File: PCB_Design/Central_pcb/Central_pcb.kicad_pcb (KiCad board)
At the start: 2 copper layers, 37 parts, among them J1 Conn_01x06_Pin, J2 Conn_01x02_Pin, J4 Conn_01x01_Pin, J7 Barrel_Jack, U3 nRF52832-QFxx, U4 BQ25171QWDRCRQ1, U5 AMS1117-3.3

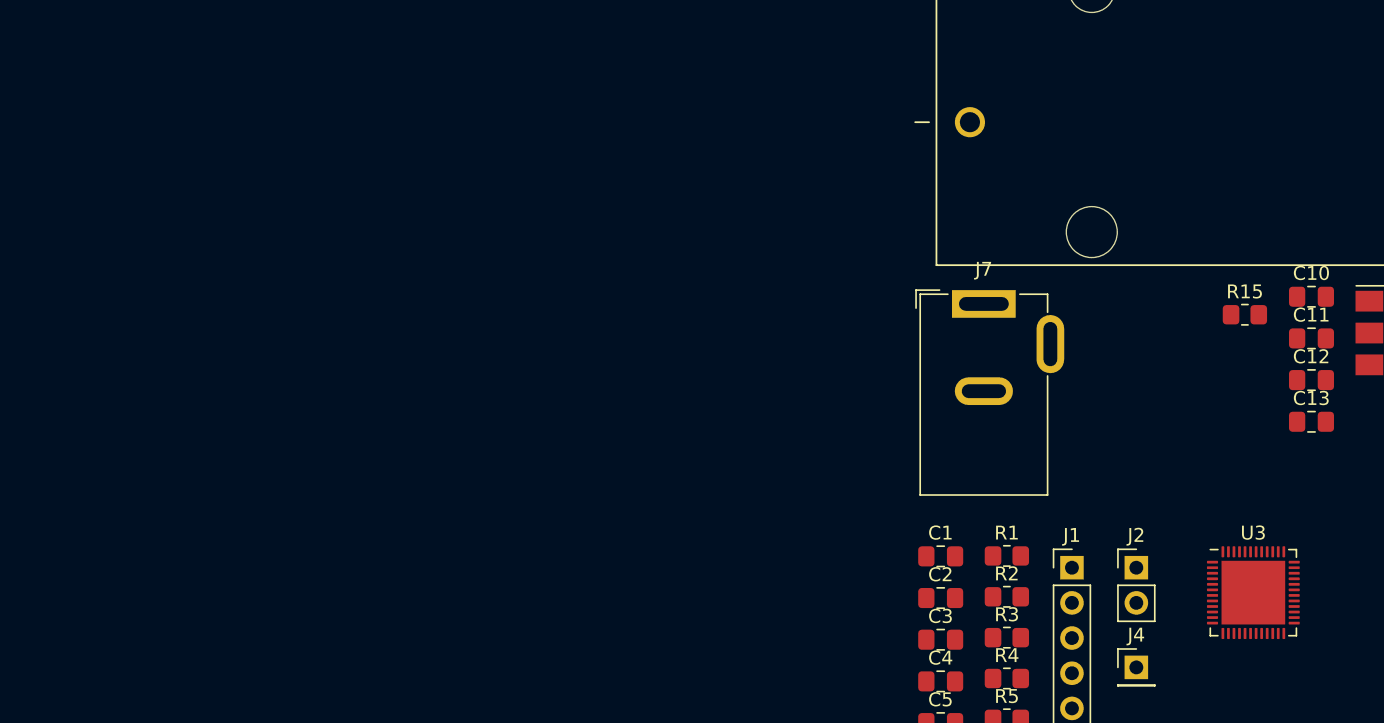
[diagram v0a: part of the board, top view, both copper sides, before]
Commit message: Scematic update
update scematic and added some footrpints
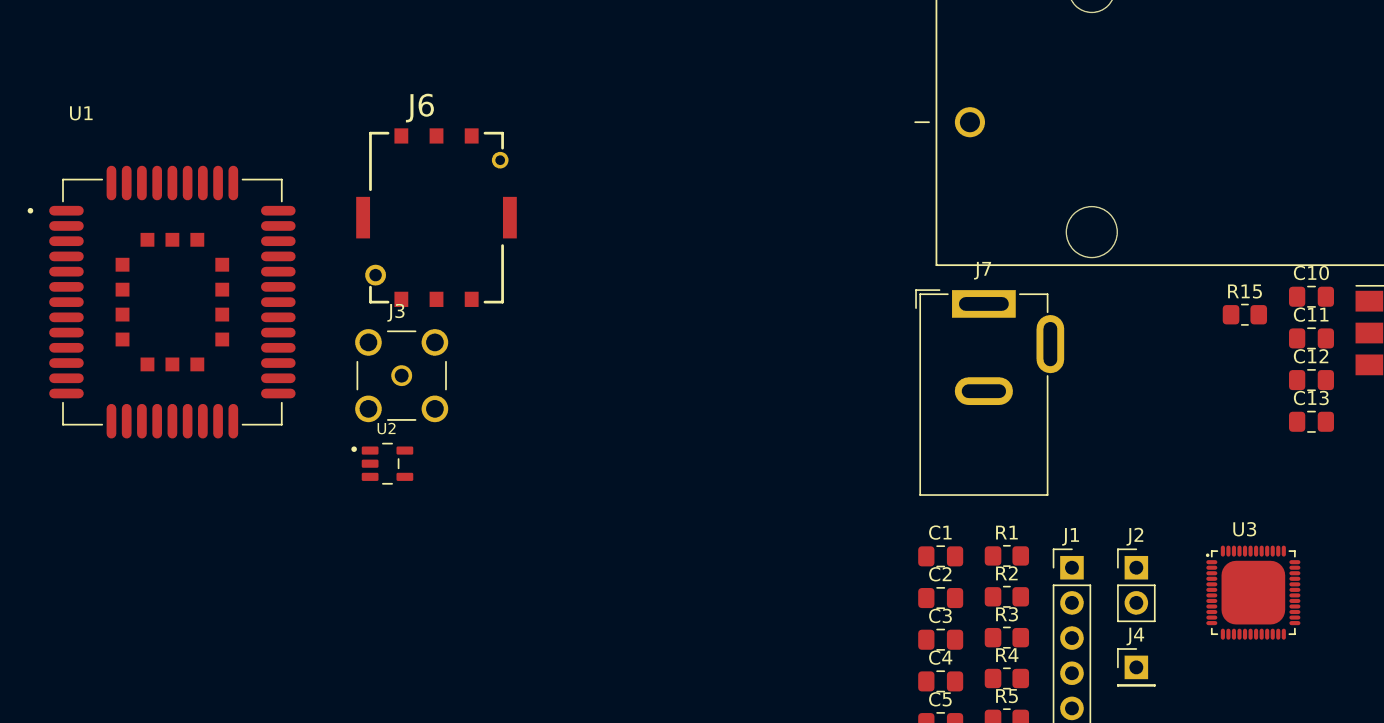
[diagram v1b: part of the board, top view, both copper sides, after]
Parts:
- added J3: SMA_CONNECTOR, Central:LPRS_SMA_CONNECTOR, F.Cu at (62.0, 116.5)
- added J6: SIM8051-6-0-14-01-X-REVD, Central:GCT_SIM8051-6-0-14-01-X-REVD, F.Cu at (64.5, 105.1)
- added U1: BC660K-GL, Central:XCVR_BC660K-GL, F.Cu at (45.4, 111.2)
- added U2: ESDS304DBVR, Central:SOT95P280X145-5N, F.Cu at (61.0, 122.9)
- D1: value LED -> STAT1
- D2: value LED -> STAT2
- U3: value nRF52832-QFxx -> NRF52832-QFAA-R; footprint Package_DFN_QFN:QFN-48-1EP_6x6mm_P0.4mm_EP4.6x4.6mm -> Central:QFN40P600X600X90-49N
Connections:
- net CE_GQ25171 renamed CE_BQ25171
- BT1 pad N1: GND -> poort45
- C1 pad 1: GND -> poort45
- C10 pad 2: GND -> poort45
- C11 pad 2: GND -> poort45
- C12 pad 1: GND -> poort45
- C13 pad 2: GND -> poort45
- C2 pad 1: GND -> poort45
- C3 pad 1: GND -> poort45
- C4 pad 1: GND -> poort45
- C5 pad 2: GND -> poort45
- C6 pad 2: GND -> poort45
- C7 pad 2: GND -> poort45
- C8 pad 2: GND -> poort45
- J7 pad 2: GND -> poort45
- R10 pad 2: GND -> poort45
- R11 pad 2: GND -> poort45
- R13 pad 2: GND -> poort45
- U3 pad 1: unconnected-(U3-DEC1-Pad1) -> Net-(U3-DEC1)
- U3 pad 13: Net-(U3-VDD-Pad13) -> +3.3V
- U3 pad 30: unconnected-(U3-ANT-Pad30) -> Net-(U3-ANT)
- U3 pad 31: Net-(U3-VSS-Pad31) -> poort45
- U3 pad 33: unconnected-(U3-DEC3-Pad33) -> Net-(U3-DEC3)
- U3 pad 34: unconnected-(U3-XC1-Pad34) -> Net-(U3-XC1)
- U3 pad 35: unconnected-(U3-XC2-Pad35) -> xc2
- U3 pad 36: Net-(U3-VDD-Pad13) -> +3.3V
- U3 pad 44: unconnected-(U3-NC-Pad44) -> (no net)
- U3 pad 45: Net-(U3-VSS-Pad31) -> poort45
- U3 pad 46: unconnected-(U3-DEC4-Pad46) -> Net-(U3-DEC4)
- U3 pad 48: Net-(U3-VDD-Pad13) -> +3.3V
- U3 pad 49: Net-(U3-VSS-Pad31) -> unconnected-(U3-EXP-Pad49)
- U4 pad 5: GND -> poort45
- U5 pad 1: GND -> poort45

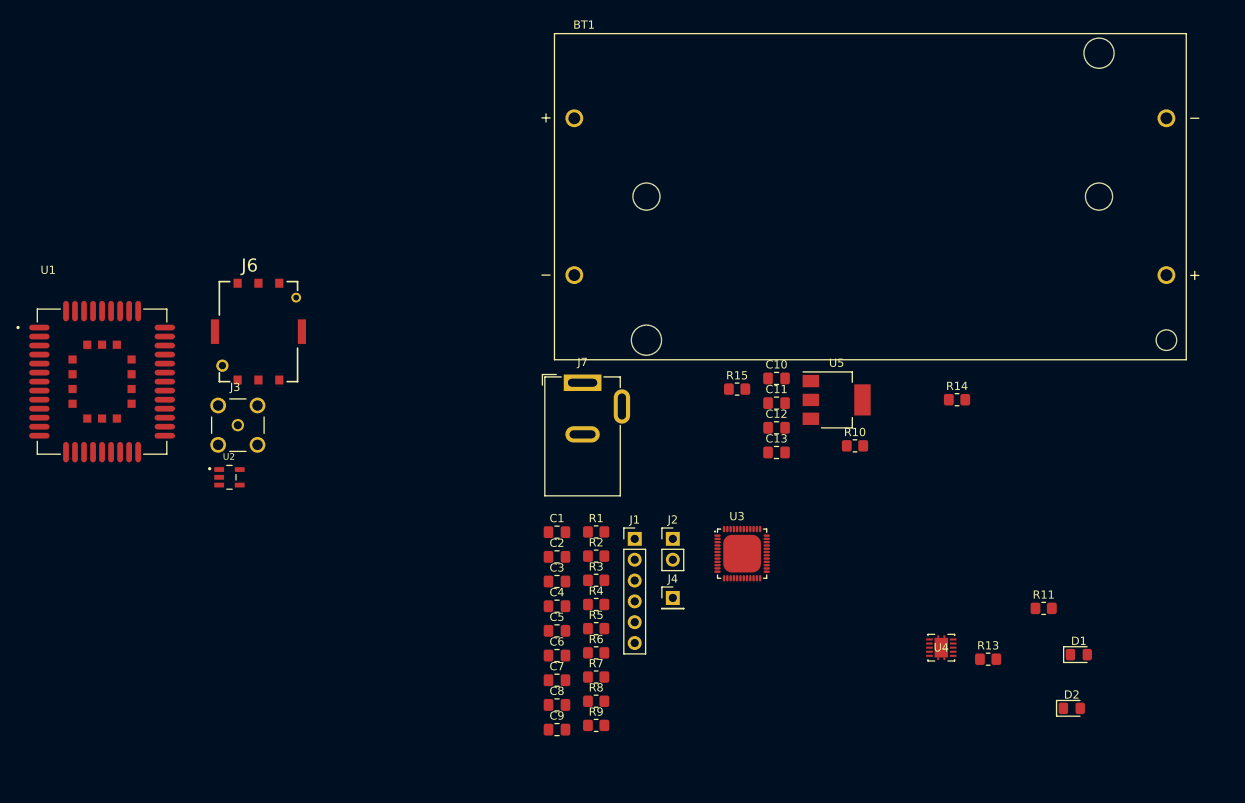
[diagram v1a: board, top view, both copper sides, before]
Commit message: Initial PCB design
Rough sketch of what the layout could be
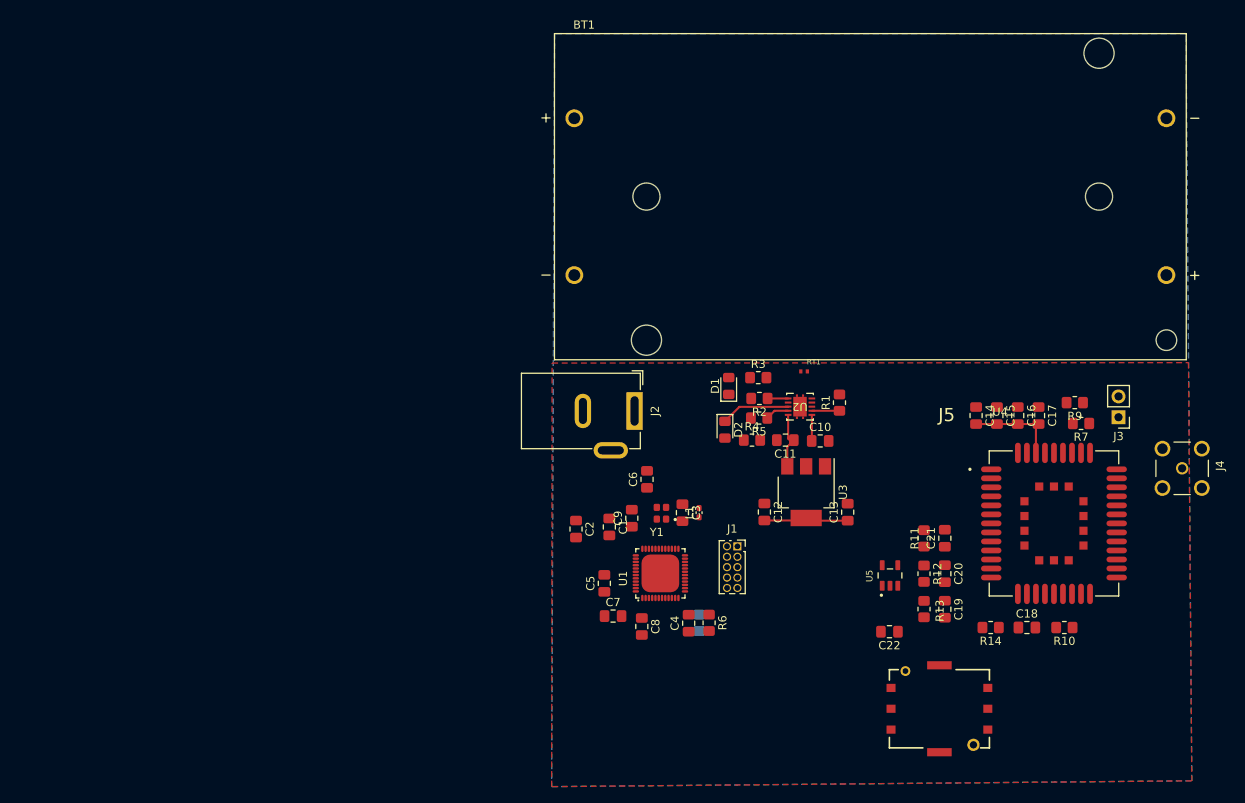
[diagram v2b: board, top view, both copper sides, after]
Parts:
- removed J6: SIM8051-6-0-14-01-X-REVD, Central:GCT_SIM8051-6-0-14-01-X-REVD
- removed J7: Barrel_Jack, Connector_BarrelJack:BarrelJack_GCT_DCJ200-10-A_Horizontal
- removed R15: 10K, Resistor_SMD:R_0805_2012Metric_Pad1.20x1.40mm_HandSolder
- added C14: 100µ, Capacitor_SMD:C_0805_2012Metric_Pad1.18x1.45mm_HandSolder, F.Cu at (152.0, 115.4)
- added C15: 100n, Capacitor_SMD:C_0805_2012Metric_Pad1.18x1.45mm_HandSolder, F.Cu at (154.6, 115.4)
- added C16: 100p, Capacitor_SMD:C_0805_2012Metric_Pad1.18x1.45mm_HandSolder, F.Cu at (157.1, 115.4)
- added C17: 22p, Capacitor_SMD:C_0805_2012Metric_Pad1.18x1.45mm_HandSolder, F.Cu at (159.7, 115.4)
- added C18: 33p, Capacitor_SMD:C_0805_2012Metric_Pad1.18x1.45mm_HandSolder, F.Cu at (158.2, 141.2)
- added C19: 33p, Capacitor_SMD:C_0805_2012Metric_Pad1.18x1.45mm_HandSolder, F.Cu at (148.2, 139.0)
- added C20: 33p, Capacitor_SMD:C_0805_2012Metric_Pad1.18x1.45mm_HandSolder, F.Cu at (148.2, 134.7)
- added C21: 33p, Capacitor_SMD:C_0805_2012Metric_Pad1.18x1.45mm_HandSolder, F.Cu at (148.2, 130.3)
- added C22: 100n, Capacitor_SMD:C_0805_2012Metric_Pad1.18x1.45mm_HandSolder, F.Cu at (141.5, 141.7)
- added J5: SIM8051-6-0-14-01-X-REVD, Central:GCT_SIM8051-6-0-14-01-X-REVD, F.Cu at (147.6, 151.1)
- added L1: 3.9n, Capacitor_SMD:C_0402_1005Metric_Pad0.74x0.62mm_HandSolder, F.Cu at (118.3, 127.2)
- added R12: 22, Resistor_SMD:R_0805_2012Metric_Pad1.20x1.40mm_HandSolder, F.Cu at (145.7, 134.7)
- added RT1: NTCG103JF103FT1, Central:THERM_NTCG103JF103FT1, F.Cu at (131.1, 110.0)
- added Y1: CX2016DB32000D0WZRC1, Central:OSCCC200X160X45N, F.Cu at (113.7, 127.3)
- C1: value 100µ -> 12pF
- C2: value 100n -> 12pF
- C3: value 100p -> 0.8p
- C4: value 22p -> 100n
- C5: value 33p -> 1u
- C6: value 33p -> 100p
- C7: value 33p -> 4.7u
- C8: value 33p -> 100n
- J1: value Conn_01x06_Pin -> Conn_ARM_JTAG_SWD_10; footprint Connector_PinHeader_2.54mm:PinHeader_1x06_P2.54mm_Vertical -> Connector_PinSocket_1.27mm:PinSocket_2x05_P1.27mm_Vertical
- J2: value Conn_01x02_Pin -> Barrel_Jack; footprint Connector_PinHeader_2.54mm:PinHeader_1x02_P2.54mm_Vertical -> Connector_BarrelJack:BarrelJack_GCT_DCJ200-10-A_Horizontal
- J3: value SMA_CONNECTOR -> Conn_01x02_Pin; footprint Central:LPRS_SMA_CONNECTOR -> Connector_PinHeader_2.54mm:PinHeader_1x02_P2.54mm_Vertical
- J4: value Conn_01x01_Pin -> SMA_CONNECTOR; footprint Connector_PinHeader_2.54mm:PinHeader_1x01_P2.54mm_Vertical -> Central:LPRS_SMA_CONNECTOR
- R1: value 1k -> 600
- R10: value 3.6K -> 1k
- R11: value 600 -> 22
- R13: value 100K -> 22
- R14: value 10K -> 10k
- R2: value 1k -> 100K
- R3, R4: value 1k -> 10K
- R5: value 1k -> 3.6K
- R6, R7: value 22 -> 1k
- R8: value 22 -> 1k; moved to B.Cu
- R9: value 10k -> 1k
- U1: value BC660K-GL -> NRF52832-QFAA-R; footprint Central:XCVR_BC660K-GL -> Central:QFN40P600X600X90-49N
- U2: value ESDS304DBVR -> BQ25171QWDRCRQ1; footprint Central:SOT95P280X145-5N -> Central:VSON10_BQ25171_3X3_TEX
- U3: value NRF52832-QFAA-R -> AMS1117-3.3; footprint Central:QFN40P600X600X90-49N -> Package_TO_SOT_SMD:SOT-223-3_TabPin2
- U4: value BQ25171QWDRCRQ1 -> BC660K-GL; footprint Central:VSON10_BQ25171_3X3_TEX -> Central:XCVR_BC660K-GL
- U5: value AMS1117-3.3 -> ESDS304DBVR; footprint Package_TO_SOT_SMD:SOT-223-3_TabPin2 -> Central:SOT95P280X145-5N
- moved J3 107.4 mm to (169.4, 115.6), turned to 180 degrees
- moved U1 72.0 mm to (113.5, 134.6), turned to 90 degrees
- moved R9 70.4 mm to (164.1, 113.8), turned to 180 degrees
- moved U2 70.1 mm to (130.6, 114.3), turned to 180 degrees
- moved R7 66.7 mm to (164.8, 116.3), turned to 180 degrees
- moved J4 64.1 mm to (177.2, 121.8), turned to -90 degrees
- moved D2 54.3 mm to (121.4, 117.1), turned to -90 degrees
- moved D1 53.8 mm to (121.9, 111.8), turned to 90 degrees
- moved R10 33.8 mm to (162.8, 141.2), turned to 180 degrees
- moved R1 33.6 mm to (135.4, 113.8), turned to 90 degrees
- moved R5 32.5 mm to (125.6, 115.7), turned to 180 degrees
- moved R3 31.7 mm to (125.5, 110.7)
- moved R14 28.1 mm to (153.8, 141.2), turned to 180 degrees
- moved R2 27.7 mm to (125.6, 113.3), turned to 180 degrees
- moved R4 27.6 mm to (124.7, 118.4)
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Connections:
- BT1 pad N1: poort45 -> GND
- BT1 pad P2: Net-(U4-OUT) -> Net-(U2-OUT)
- C1 pad 1: poort45 -> GND
- C1 pad 2: +3.3V -> Net-(U1-XC1)
- C10 pad 1: Net-(U4-IN) -> Net-(U2-IN)
- C10 pad 2: poort45 -> GND
- C11 pad 1: Net-(U4-OUT) -> Net-(U2-OUT)
- C11 pad 2: poort45 -> GND
- C12 pad 1: poort45 -> GND
- C13 pad 2: poort45 -> GND
- C2 pad 1: poort45 -> GND
- C2 pad 2: +3.3V -> xc2
- C3 pad 1: poort45 -> GND
- C3 pad 2: +3.3V -> Net-(U1-ANT)
- C4 pad 1: poort45 -> +3.3V
- C4 pad 2: +3.3V -> GND
- C5 pad 1: Net-(J6-VCC) -> Net-(U1-DEC4)
- C5 pad 2: poort45 -> GND
- C6 pad 1: Net-(U1-USIM_CLK) -> Net-(U1-DEC3)
- C6 pad 2: poort45 -> GND
- C7 pad 1: Net-(U1-USIM_RST) -> GND
- C7 pad 2: poort45 -> +3.3V
- C8 pad 1: Net-(U1-USIM_DATA) -> Net-(U1-DEC1)
- C8 pad 2: poort45 -> GND
- C9 pad 1: Net-(J6-GND) -> +3.3V
- C9 pad 2: Net-(J6-VCC) -> GND
- J1 pad 1: Net-(J1-Pin_1) -> +3.3V
- J1 pad 2: Net-(J1-Pin_2) -> Net-(J1-SWDIO/TMS)
- J1 pad 3: Net-(J1-Pin_3) -> GND
- J1 pad 4: Net-(J1-Pin_4) -> Net-(J1-SWDCLK/TCK)
- J1 pad 5: Net-(J1-Pin_5) -> GND
- J1 pad 6: Net-(J1-Pin_6) -> SW0
- J2 pad 1: Net-(J2-Pin_1) -> Net-(U2-IN)
- J2 pad 2: Net-(J2-Pin_2) -> GND
- J3 pad 1: Net-(U1-ANT_RF) -> Net-(J3-Pin_1)
- J4 pad 1: Net-(J4-Pin_1) -> Net-(U4-ANT_RF)
- R1 pad 1: Net-(J2-Pin_1) -> Net-(U2-ISET)
- R1 pad 2: Net-(U1-DBG_RXD) -> GND
- R10 pad 1: Net-(U4-VSET) -> Net-(U4-RI)
- R10 pad 2: poort45 -> RI_BC660
- R11 pad 1: Net-(U4-ISET) -> Net-(U4-USIM_DATA)
- R11 pad 2: poort45 -> Net-(J5-I/O)
- R13 pad 1: Net-(U4-CHM_TMP) -> Net-(U4-USIM_CLK)
- R13 pad 2: poort45 -> Net-(J5-CLK)
- R14 pad 1: Net-(D1-A) -> Net-(J5-VCC)
- R14 pad 2: +3.3V -> Net-(J5-I/O)
- R2 pad 1: Net-(J1-Pin_3) -> Net-(U2-CHM_TMP)
- R2 pad 2: Net-(U1-MAIN_TXD) -> GND
- R3 pad 1: Net-(J1-Pin_4) -> Net-(D1-A)
- R3 pad 2: Net-(U1-MAIN_RXD) -> +3.3V
- R4 pad 1: Net-(J2-Pin_2) -> Net-(D2-A)
- R4 pad 2: Net-(U1-DBG_TXD) -> +3.3V
- R5 pad 1: Net-(U1-RI) -> Net-(U2-VSET)
- R5 pad 2: Net-(J1-Pin_6) -> GND
- R6 pad 1: Net-(U1-USIM_CLK) -> TXD_BC660
- R6 pad 2: Net-(J6-CLK) -> Net-(U4-MAIN_TXD)
- R7 pad 1: Net-(U1-USIM_RST) -> Net-(J3-Pin_1)
- R7 pad 2: Net-(J6-RST) -> Net-(U4-DBG_RXD)
- R8 pad 1: Net-(U1-USIM_DATA) -> RXD_BC660
- R8 pad 2: Net-(J6-I/O) -> Net-(U4-MAIN_RXD)
- R9 pad 1: Net-(J6-VCC) -> Net-(J3-Pin_2)
- R9 pad 2: Net-(J6-I/O) -> Net-(U4-DBG_TXD)
- U1 pad 1: poort45 -> Net-(U1-DEC1)
- U1 pad 10: Net-(J6-GND) -> BOOT_BC660
- U1 pad 11: Net-(U1-USIM_DATA) -> unconnected-(U1-P0.09-Pad11)
- U1 pad 12: Net-(U1-USIM_RST) -> unconnected-(U1-P0.10-Pad12)
- U1 pad 13: Net-(U1-USIM_CLK) -> +3.3V
- U1 pad 14: Net-(J6-VCC) -> RXD_BC660
- U1 pad 15: Net-(J1-Pin_1) -> TXD_BC660
- U1 pad 16: Net-(J1-Pin_2) -> RI_BC660
- U1 pad 17: Net-(U1-MAIN_TXD) -> PSM_EINT_BC660
- U1 pad 18: Net-(U1-MAIN_RXD) -> unconnected-(U1-P0.15-Pad18)
- U1 pad 19: Net-(J1-Pin_5) -> unconnected-(U1-P0.16-Pad19)
- U1 pad 20: Net-(U1-RI) -> unconnected-(U1-P0.17-Pad20)
- U1 pad 21: unconnected-(U1-RESERVED_1-Pad21) -> SW0
- U1 pad 24: unconnected-(U1-VDD_EXT-Pad24) -> Nreset
- U1 pad 25: unconnected-(U1-RESERVED_1-Pad25) -> Net-(J1-SWDCLK/TCK)
- U1 pad 26: unconnected-(U1-RESERVED_1-Pad26) -> Net-(J1-SWDIO/TMS)
- U1 pad 27: poort45 -> unconnected-(U1-P0.22-Pad27)
- U1 pad 30: unconnected-(U1-RESERVED_1-Pad30) -> Net-(U1-ANT)
- U1 pad 31: unconnected-(U1-RESERVED_1-Pad31) -> GND
- U1 pad 33: unconnected-(U1-RESERVED_1-Pad33) -> Net-(U1-DEC3)
- U1 pad 34: poort45 -> Net-(U1-XC1)
- U1 pad 35: Net-(U1-ANT_RF) -> xc2
- U1 pad 36: poort45 -> +3.3V
- U1 pad 37: poort45 -> unconnected-(U1-P0.25-Pad37)
- U1 pad 38: Net-(U1-DBG_RXD) -> unconnected-(U1-P0.26-Pad38)
- U1 pad 39: Net-(U1-DBG_TXD) -> unconnected-(U1-P0.27-Pad39)
- U1 pad 40: poort45 -> unconnected-(U1-P0.28-Pad40)
- U1 pad 41: poort45 -> unconnected-(U1-P0.29-Pad41)
- U1 pad 42: +3.3V -> unconnected-(U1-P0.30-Pad42)
- U1 pad 43: +3.3V -> unconnected-(U1-P0.31-Pad43)
- U1 pad 44: unconnected-(U1-RESERVED_1-Pad44) -> (no net)
- U1 pad 45: unconnected-(U1-RESERVED_1-Pad45) -> GND
- U1 pad 46: unconnected-(U1-RESERVED_2-Pad46) -> Net-(U1-DEC4)
- U1 pad 48: unconnected-(U1-RESERVED_2-Pad48) -> +3.3V
- U1 pad 7: Net-(J4-Pin_1) -> unconnected-(U1-P0.05-Pad7)
- U1 pad 9: unconnected-(U1-ADC0-Pad9) -> RESET_BC660
- U2 pad 1: Net-(J6-VCC) -> Net-(U2-IN)
- U2 pad 2: poort45 -> Net-(U2-ISET)
- U2 pad 3: Net-(U1-USIM_CLK) -> CE_BQ25171
- U2 pad 4: Net-(U1-USIM_RST) -> Net-(U2-TS)
- U2 pad 5: Net-(U1-USIM_DATA) -> GND
- U3 pad 1: Net-(U3-DEC1) -> GND
- U3 pad 2: unconnected-(U3-P0.00-Pad2) -> +3.3V
- U3 pad 3: unconnected-(U3-P0.01-Pad3) -> Net-(U2-OUT)
- U4 pad 1: Net-(U4-IN) -> GND
- U4 pad 10: Net-(U4-OUT) -> Net-(J5-GND)
- U4 pad 11: unconnected-(U4-Pad11) -> Net-(U4-USIM_DATA)
- U4 pad 2: Net-(U4-ISET) -> unconnected-(U4-RESERVED_1-Pad2)
- U4 pad 3: CE_BQ25171 -> unconnected-(U4-GPIO1-Pad3)
- U4 pad 4: Net-(U4-TS) -> unconnected-(U4-GPIO2-Pad4)
- U4 pad 5: poort45 -> unconnected-(U4-GPIO3-Pad5)
- U4 pad 6: Net-(U4-CHM_TMP) -> unconnected-(U4-GPIO4-Pad6)
- U4 pad 7: Net-(D1-K) -> BOOT_BC660
- U4 pad 8: Net-(D2-K) -> unconnected-(U4-RESERVED_1-Pad8)
- U4 pad 9: Net-(U4-VSET) -> unconnected-(U4-ADC0-Pad9)
- U5 pad 1: poort45 -> Net-(J5-VCC)
- U5 pad 2: +3.3V -> GND
- U5 pad 3: Net-(U4-OUT) -> Net-(U4-USIM_CLK)
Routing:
- net +3.3V: track 0.00 -> 20.3 mm
- net Net-(D2-K): track 0.00 -> 8.45 mm
- net Net-(U2-OUT): track 0.00 -> 6.69 mm
- net Net-(U2-ISET): track 0.00 -> 3.37 mm
- net Net-(U2-IN): track 0.00 -> 3.16 mm
- net Net-(U2-VSET): track 0.00 -> 2.91 mm
- net Net-(U2-CHM_TMP): track 0.00 -> 2.51 mm
- added copper zone on B.Cu, net GND
- added copper zone on F.Cu, net GND

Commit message: PCB route
Volledig geroute nog juist controleren en mounting holes doen + controleren dat er overal gnd en 3.3v mooi verbonden is
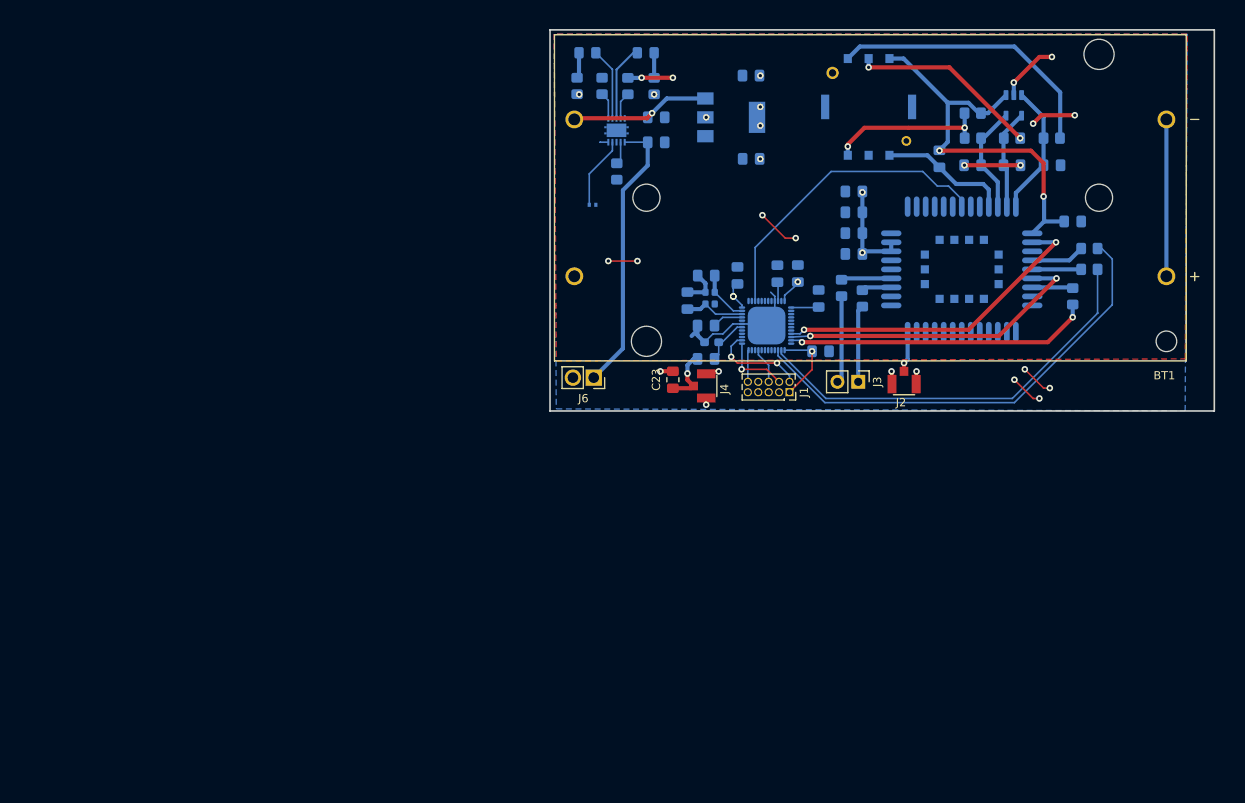
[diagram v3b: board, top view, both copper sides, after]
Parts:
- added C23: 1.2pF, Capacitor_SMD:C_0805_2012Metric_Pad1.18x1.45mm_HandSolder, F.Cu at (115.1, 111.0)
- added J6: Conn_01x02_Pin, Connector_PinSocket_2.54mm:PinSocket_1x02_P2.54mm_Vertical, F.Cu at (105.4, 110.7)
- C1, C10, C11, C12, C13, C14, C15, C16, C17, C18, C19, C2, C20, C21, C22, C4, C5, C6, C7, C8, C9, D1, D2, R10, R11, R12, R13, R14, R2, R3, R4, R5, R6, R7, R9, RT1, U1, U2, U3, U4, U5, Y1: moved to B.Cu
- C3: footprint Capacitor_SMD:C_0805_2012Metric_Pad1.18x1.45mm_HandSolder -> Capacitor_SMD:C_0603_1608Metric_Pad1.08x0.95mm_HandSolder; moved to B.Cu
- J2: value Barrel_Jack -> U.FL-R-SMT_01_; footprint Connector_BarrelJack:BarrelJack_GCT_DCJ200-10-A_Horizontal -> Central:HRS_U.FL-R-SMT_01_
- J4: value SMA_CONNECTOR -> U.FL-R-SMT_01_; footprint Central:LPRS_SMA_CONNECTOR -> Central:HRS_U.FL-R-SMT_01_
- J5: value SIM8051-6-0-14-01-X-REVD -> SIM; moved to B.Cu
- L1: footprint Capacitor_SMD:C_0402_1005Metric_Pad0.74x0.62mm_HandSolder -> Capacitor_SMD:C_0805_2012Metric_Pad1.18x1.45mm_HandSolder; moved to B.Cu
- R1: value 600 -> 3k; moved to B.Cu
- moved J5 73.9 mm to (138.9, 77.7), turned to 0 degrees
- moved R6 65.1 mm to (165.9, 95.0), turned to 180 degrees
- moved R8 64.2 mm to (165.9, 97.5), turned to 180 degrees
- moved R14 62.8 mm to (151.6, 78.5)
- moved R13 59.5 mm to (161.3, 81.5), turned to 0 degrees
- moved U5 59.3 mm to (156.6, 77.5), turned to -90 degrees
- moved J4 58.9 mm to (119.1, 111.8)
- moved C22 58.0 mm to (147.6, 84.1), turned to 90 degrees
- moved C19 55.7 mm to (161.3, 84.8), turned to 0 degrees
- moved R12 54.2 mm to (156.4, 81.5), turned to 0 degrees
- moved C12 53.3 mm to (124.6, 73.9), turned to 0 degrees
- moved C20 50.5 mm to (156.4, 84.8), turned to 0 degrees
- moved C18 49.8 mm to (163.8, 91.7)
- moved R11 49.2 mm to (151.7, 81.5), turned to 180 degrees
- moved C7 47.5 mm to (130.3, 98.0), turned to -90 degrees
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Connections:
- BT1 pad N1: GND -> Net-(BT1-PadN1)
- BT1 pad N2: Net-(BT1-PadN2) -> GND
- BT1 pad P1: Net-(BT1-PadN2) -> Net-(U2-OUT)
- BT1 pad P2: Net-(U2-OUT) -> Net-(BT1-PadN1)
- C10 pad 1: Net-(U2-IN) -> Net-(J6-Pin_1)
- J2 pad 1: Net-(U2-IN) -> GND
- J2 pad 3: (no net) -> Net-(J2-SIG)
- J4 pad 1: Net-(U4-ANT_RF) -> GND
- L1 pad 2: RF -> Net-(J4-SIG)
- U1 pad 10: BOOT_BC660 -> PSM_EINT_BC660
- U1 pad 11: unconnected-(U1-P0.09-Pad11) -> RI_BC660
- U1 pad 16: RI_BC660 -> unconnected-(U1-P0.13-Pad16)
- U1 pad 17: PSM_EINT_BC660 -> unconnected-(U1-P0.14-Pad17)
- U1 pad 39: unconnected-(U1-P0.27-Pad39) -> BOOT_BC660
- U1 pad 49: unconnected-(U1-EXP-Pad49) -> GND
- U2 pad 1: Net-(U2-IN) -> Net-(J6-Pin_1)
- U4 pad 35: Net-(U4-ANT_RF) -> Net-(J2-SIG)
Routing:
- net GND: track 0.00 -> 72.2 mm, vias 0 -> 21
- net TXD_BC660: track 0.00 -> 56.7 mm
- net RXD_BC660: track 0.00 -> 51.0 mm
- net Net-(J5-VCC): track 0.00 -> 49.1 mm, vias 0 -> 2
- net RESET_BC660: track 0.00 -> 39.8 mm, vias 0 -> 2
- net PSM_EINT_BC660: track 0.00 -> 38.2 mm, vias 0 -> 2
- net BOOT_BC660: track 0.00 -> 37.9 mm
- net RI_BC660: track 0.00 -> 37.3 mm, vias 0 -> 2
- net Net-(J5-CLK): track 0.00 -> 34.4 mm
- net Net-(J6-Pin_1): track 0.00 -> 34.2 mm
- net Net-(J5-RST): track 0.00 -> 23.1 mm, vias 0 -> 2
- net Net-(J5-I/O): track 0.00 -> 19.2 mm, vias 0 -> 2
- net Net-(BT1-PadN1): track 0.00 -> 19.1 mm
- net Net-(U4-USIM_CLK): track 0.00 -> 16.1 mm
- net Net-(J5-GND): track 0.00 -> 15.9 mm
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- added copper zone on F.Cu, net +3.3V
- removed copper zone on F.Cu, net GND
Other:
- board outline added: 81 x 46.5 mm

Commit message: Minur PCB update
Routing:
- net GND: track 72.2 -> 83.7 mm
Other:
- board size 81 x 46.5 mm -> 81.8 x 46.5 mm
- board text added: "Iot systems by:Jarno de Jonckheere, Jonathan Gheysens en Emiel Dever V1.0"
